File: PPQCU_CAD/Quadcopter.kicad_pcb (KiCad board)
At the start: 2 copper layers, 135.6 x 80.8 mm, 155 parts, among them P1 Battery, P10 CONN_02X04, P2 DEBUG, P3 Serv1, P4 Serv2, P5 Serv3, P6 Serv4, P7 SecServ1, P8 SecServ2, P9 ws2812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

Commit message: Fixed spelling error
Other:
- board text added: "Philipp Schilk Quadcopter Controller Production 1 PP 2015/16"
- board text removed: "Philipp Schilk Quadcopter Controler Production 1 PP 2015/16"
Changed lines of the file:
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@@
       (drillshape 0)
       (scaleselection 1)
-      (outputdirectory "C:"))
+      (outputdirectory C:))
   )
   (net 0 "")
@@
     (effects (font (size 1.5 1.5) (thickness 0.3)))
   )
-  (gr_text "Philipp Schilk\n\nQuadcopter Controler Production 1\n\nPP 2015/16\n" (at 169.7355 104.267) (layer B.SilkS)
+  (gr_text "Philipp Schilk\n\nQuadcopter Controller Production 1\n\nPP 2015/16\n" (at 169.7355 104.267) (layer B.SilkS)
     (effects (font (size 1.5 1.5) (thickness 0.3)) (justify mirror))
   )

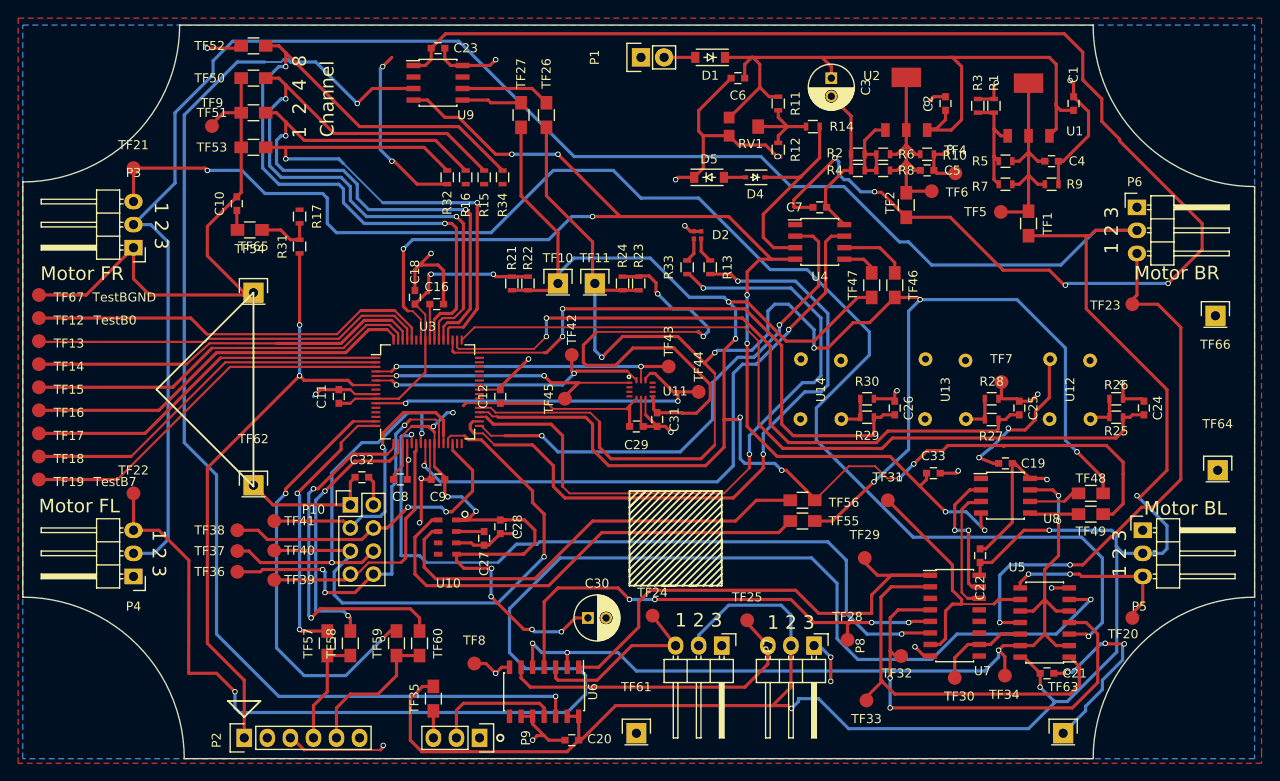
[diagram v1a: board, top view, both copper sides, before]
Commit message: Fixed small overlaps/visual errors in layout
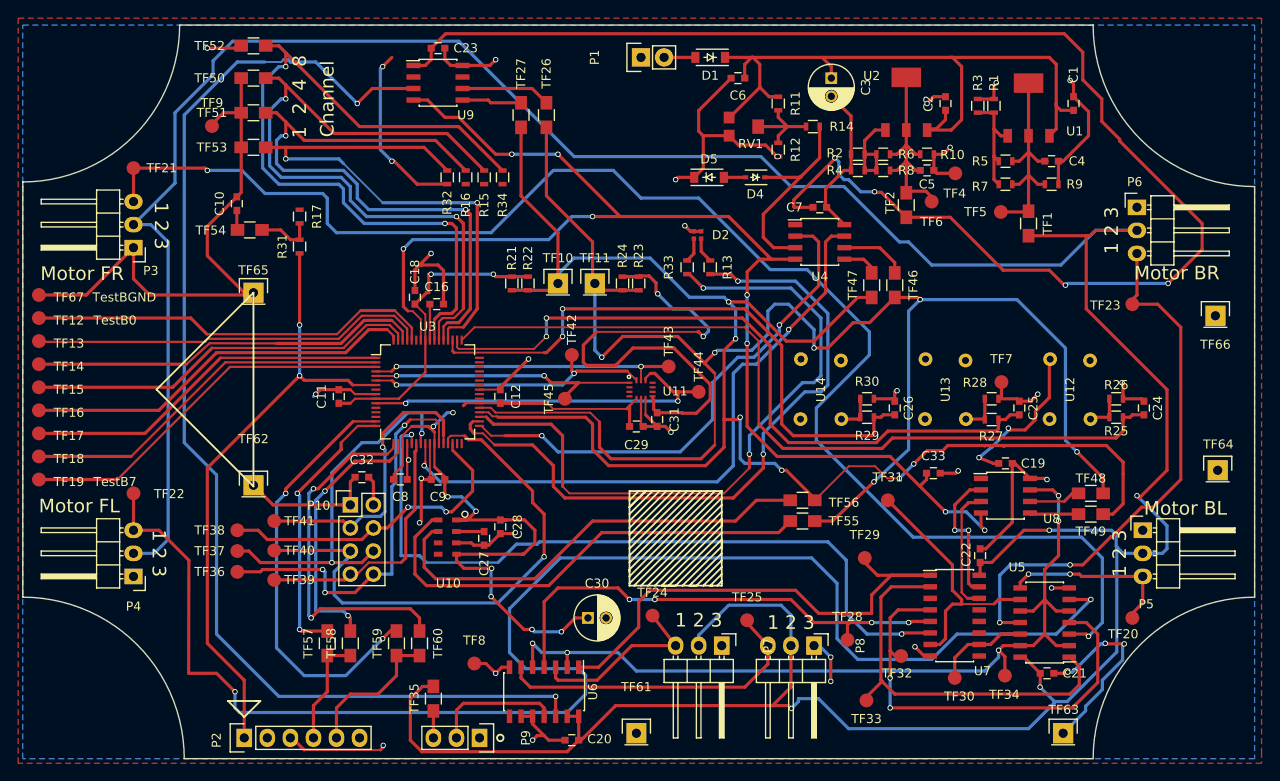
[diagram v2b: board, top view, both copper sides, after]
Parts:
- moved TF6 1.14 mm to (180.7, 72.9)
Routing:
- net Net-(C5-Pad1): track 24.2 -> 24.9 mm
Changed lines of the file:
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@@
     (links 304)
     (no_connects 0)
-    (area 80.137 52.705 217.043001 135.061333)
+    (area 80.569999 53.391999 216.356001 134.314001)
     (thickness 1.6)
     (drawings 91)
-    (tracks 1550)
+    (tracks 1552)
     (zones 0)
     (modules 155)
@@
     (32 B.Adhes user)
     (33 F.Adhes user)
-    (34 B.Paste user hide)
+    (34 B.Paste user)
     (35 F.Paste user hide)
     (36 B.SilkS user)
-    (37 F.SilkS user hide)
+    (37 F.SilkS user)
     (38 B.Mask user)
     (39 F.Mask user)
@@
     (tags "capacitor 0603")
     (attr smd)
-    (fp_text reference C5 (at 2.794 0) (layer F.SilkS)
+    (fp_text reference C5 (at 0 1.524) (layer F.SilkS)
       (effects (font (size 1 1) (thickness 0.15)))
     )
@@
     (tags "capacitor 0603")
     (attr smd)
-    (fp_text reference C12 (at 0 -1.9 90) (layer F.SilkS)
+    (fp_text reference C12 (at 0 1.7145 90) (layer F.SilkS)
       (effects (font (size 1 1) (thickness 0.15)))
     )
@@
     (tags "capacitor 0603")
     (attr smd)
-    (fp_text reference C22 (at -3.556 0 90) (layer F.SilkS)
+    (fp_text reference C22 (at 0.127 -1.524 90) (layer F.SilkS)
       (effects (font (size 1 1) (thickness 0.15)))
     )
@@
     (descr "Through hole pin header")
     (tags "pin header")
-    (fp_text reference P3 (at 0 8.255 180) (layer F.SilkS)
+    (fp_text reference P3 (at -1.905 -2.54 180) (layer F.SilkS)
       (effects (font (size 1 1) (thickness 0.15)))
     )
@@
     (descr "Through hole pin header")
     (tags "pin header")
-    (fp_text reference P5 (at -0.381 8.382) (layer F.SilkS)
+    (fp_text reference P5 (at 0.381 8.128) (layer F.SilkS)
       (effects (font (size 1 1) (thickness 0.15)))
     )
@@
     (descr "Through hole pin header")
     (tags "pin header")
-    (fp_text reference P10 (at -4.064 0.508) (layer F.SilkS)
+    (fp_text reference P10 (at -3.4925 0.0635) (layer F.SilkS)
       (effects (font (size 1 1) (thickness 0.15)))
     )
@@
     (tags "resistor 0603")
     (attr smd)
-    (fp_text reference R10 (at 3.048 0.127) (layer F.SilkS)
+    (fp_text reference R10 (at 2.794 0.0635) (layer F.SilkS)
       (effects (font (size 1 1) (thickness 0.15)))
     )
@@
     (tags "resistor 0603")
     (attr smd)
-    (fp_text reference R28 (at 0 -1.9) (layer F.SilkS)
+    (fp_text reference R28 (at -1.8415 -1.778) (layer F.SilkS)
       (effects (font (size 1 1) (thickness 0.15)))
     )
@@
   )
   (module Measurement_Points:Measurement_Point_Round-SMD-Pad_Small (layer F.Cu)
-    (at 180.721 71.755)
+    (at 180.721 72.898)
     (descr "Mesurement Point, Round, SMD Pad, DM 1.5mm,")
     (tags "Mesurement Point, Round, SMD Pad, DM 1.5mm,")
-    (fp_text reference TF6 (at 2.794 0.127) (layer F.SilkS)
+    (fp_text reference TF6 (at 0 2.2225) (layer F.SilkS)
       (effects (font (size 1 1) (thickness 0.15)))
     )
@@
     (descr "Mesurement Point, Round, SMD Pad, DM 1.5mm,")
     (tags "Mesurement Point, Round, SMD Pad, DM 1.5mm,")
-    (fp_text reference TF21 (at 0 -2.54) (layer F.SilkS)
+    (fp_text reference TF21 (at 3.1115 0) (layer F.SilkS)
       (effects (font (size 1 1) (thickness 0.15)))
     )
@@
     (descr "Mesurement Point, Round, SMD Pad, DM 1.5mm,")
     (tags "Mesurement Point, Round, SMD Pad, DM 1.5mm,")
-    (fp_text reference TF22 (at 0 -2.54) (layer F.SilkS)
+    (fp_text reference TF22 (at 3.937 0.0635) (layer F.SilkS)
       (effects (font (size 1 1) (thickness 0.15)))
     )
@@
     (tags "resistor 0805")
     (attr smd)
-    (fp_text reference TF54 (at 0 -2.1 180) (layer F.SilkS)
+    (fp_text reference TF54 (at 4.2926 -0.0508 180) (layer F.SilkS)
       (effects (font (size 1 1) (thickness 0.15)))
     )
@@
     (descr "Through hole pin header")
     (tags "pin header")
-    (fp_text reference TF63 (at 0 -5.1) (layer F.SilkS)
+    (fp_text reference TF63 (at 0.0635 -2.6035) (layer F.SilkS)
       (effects (font (size 1 1) (thickness 0.15)))
     )
@@
     (descr "Through hole pin header")
     (tags "pin header")
-    (fp_text reference TF64 (at 0 -5.1) (layer F.SilkS)
+    (fp_text reference TF64 (at 0.0635 -2.8575) (layer F.SilkS)
       (effects (font (size 1 1) (thickness 0.15)))
     )
@@
     (descr "Through hole pin header")
     (tags "pin header")
-    (fp_text reference TF65 (at 0 -5.1) (layer F.SilkS)
+    (fp_text reference TF65 (at 0 -2.4765) (layer F.SilkS)
       (effects (font (size 1 1) (thickness 0.15)))
     )
@@
     (descr "Mesurement Point, Round, SMD Pad, DM 1.5mm,")
     (tags "Mesurement Point, Round, SMD Pad, DM 1.5mm,")
-    (fp_text reference TF4 (at 0 -2.54) (layer F.SilkS)
+    (fp_text reference TF4 (at -0.0635 2.2225) (layer F.SilkS)
       (effects (font (size 1 1) (thickness 0.15)))
     )
@@
   (segment (start 190.373 68.453) (end 191.389 67.437) (width 0.3516) (layer F.Cu) (net 3))
   (segment (start 191.389 67.437) (end 191.389 65.659) (width 0.3516) (layer F.Cu) (net 3) (status 20))
+  (segment (start 180.721 72.898) (end 180.721 72.39) (width 0.3516) (layer F.Cu) (net 4) (status C00000))
+  (segment (start 180.721 72.39) (end 180.086 71.755) (width 0.3516) (layer F.Cu) (net 4) (status 400000))
   (segment (start 177.927 71.929) (end 177.927 68.453) (width 0.3516) (layer F.Cu) (net 4) (status 10))
   (segment (start 177.927 65.024) (end 177.927 59.224) (width 0.3516) (layer F.Cu) (net 4) (status 30))
-  (segment (start 180.721 71.755) (end 178.101 71.755) (width 0.3516) (layer F.Cu) (net 4) (status 30))
+  (segment (start 180.086 71.755) (end 178.101 71.755) (width 0.3516) (layer F.Cu) (net 4) (status 30))
   (segment (start 178.181 66.929) (end 177.927 66.675) (width 0.3516) (layer F.Cu) (net 4))
   (segment (start 179.463 69.469) (end 178.943 69.469) (width 0.3516) (layer F.Cu) (net 4) (status 10))
